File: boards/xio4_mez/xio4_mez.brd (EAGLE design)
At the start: 63 x 91 mm, 89 parts, among them IC1 SN74LVC2G07DCKR, IC2 SN74LVC1G07MDCKREP, IC3 NL17SZ126XV5T2G, IC4 TPS2051BDBVR, Q1 SMMBT3904LT1G

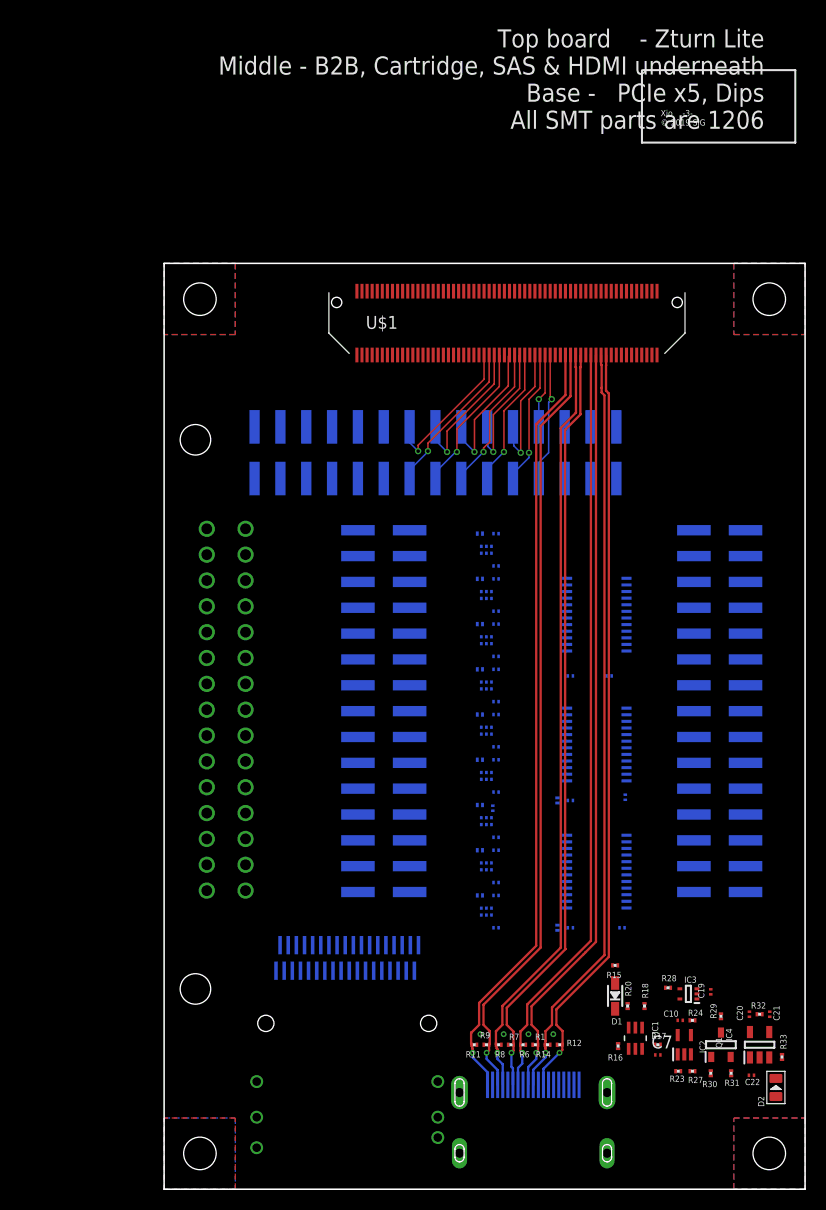
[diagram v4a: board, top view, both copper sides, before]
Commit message: Almost routed. Fixed tx100 net classes
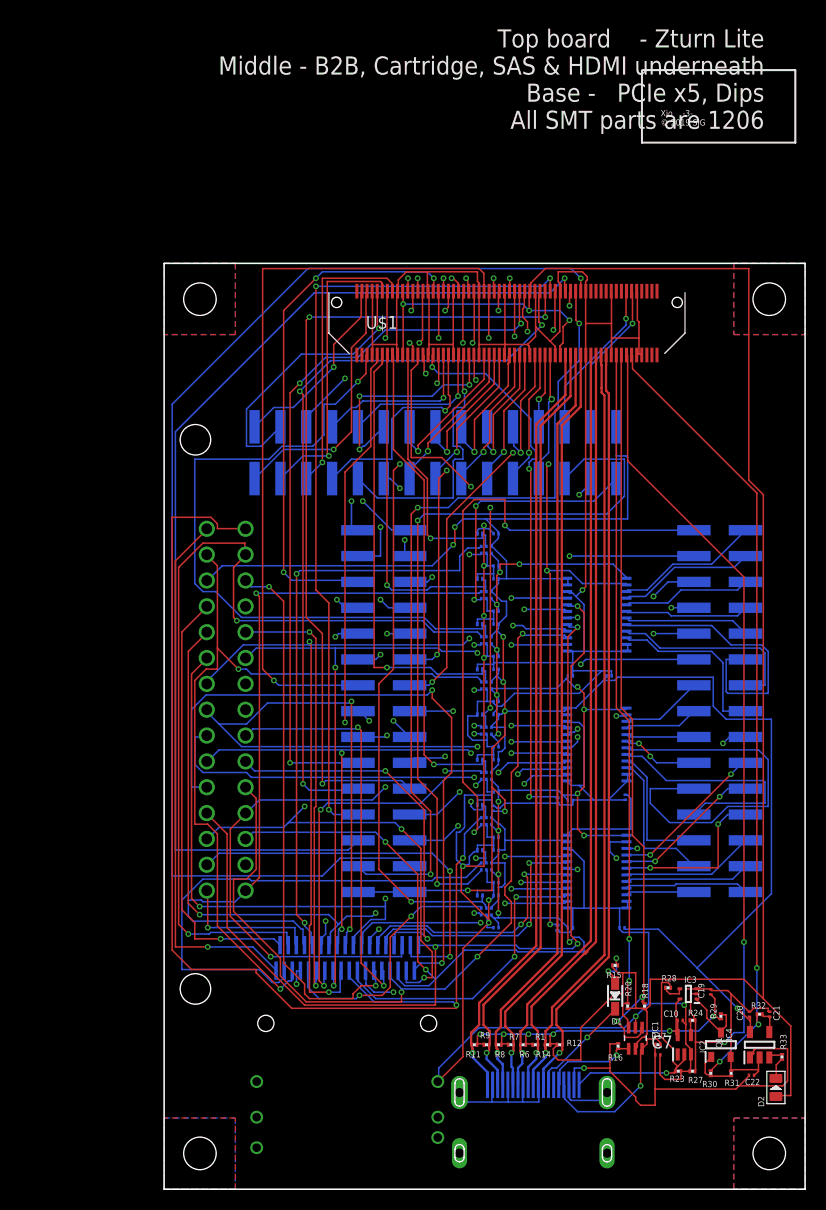
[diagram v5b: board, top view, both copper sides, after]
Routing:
- net GND: track 0.00 -> 444.9 mm, vias 0 -> 10
- net +5V: track 0.00 -> 240.1 mm, vias 0 -> 8
- net VCCIO: track 0.00 -> 219.8 mm, vias 4 -> 9
- net HBUS27: track 0.00 -> 118.1 mm, vias 0 -> 1
- net HI_CLK: track 0.00 -> 113.2 mm, vias 0 -> 2
- net +3V3: track 0.00 -> 107.7 mm, vias 0 -> 14
- net HBUS24: track 0.00 -> 105.3 mm, vias 0 -> 1
- net HI_A3: track 0.00 -> 97.5 mm, vias 0 -> 3
- net HI_A1: track 0.00 -> 92.9 mm, vias 0 -> 3
- net HI_R/!W!: track 0.00 -> 88.0 mm, vias 0 -> 2
- net HI_A6: track 0.00 -> 86.5 mm, vias 0 -> 3
- net HI_A4: track 0.00 -> 86.1 mm, vias 0 -> 4
- net HI_D1: track 0.00 -> 85.9 mm, vias 0 -> 4
- net HDMI_DET_IO: track 0.00 -> 85.0 mm, vias 0 -> 2
- net DIR_A: track 0.00 -> 84.4 mm, vias 0 -> 5
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- added copper zone on layer 2, net GND

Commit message: Fully routed board
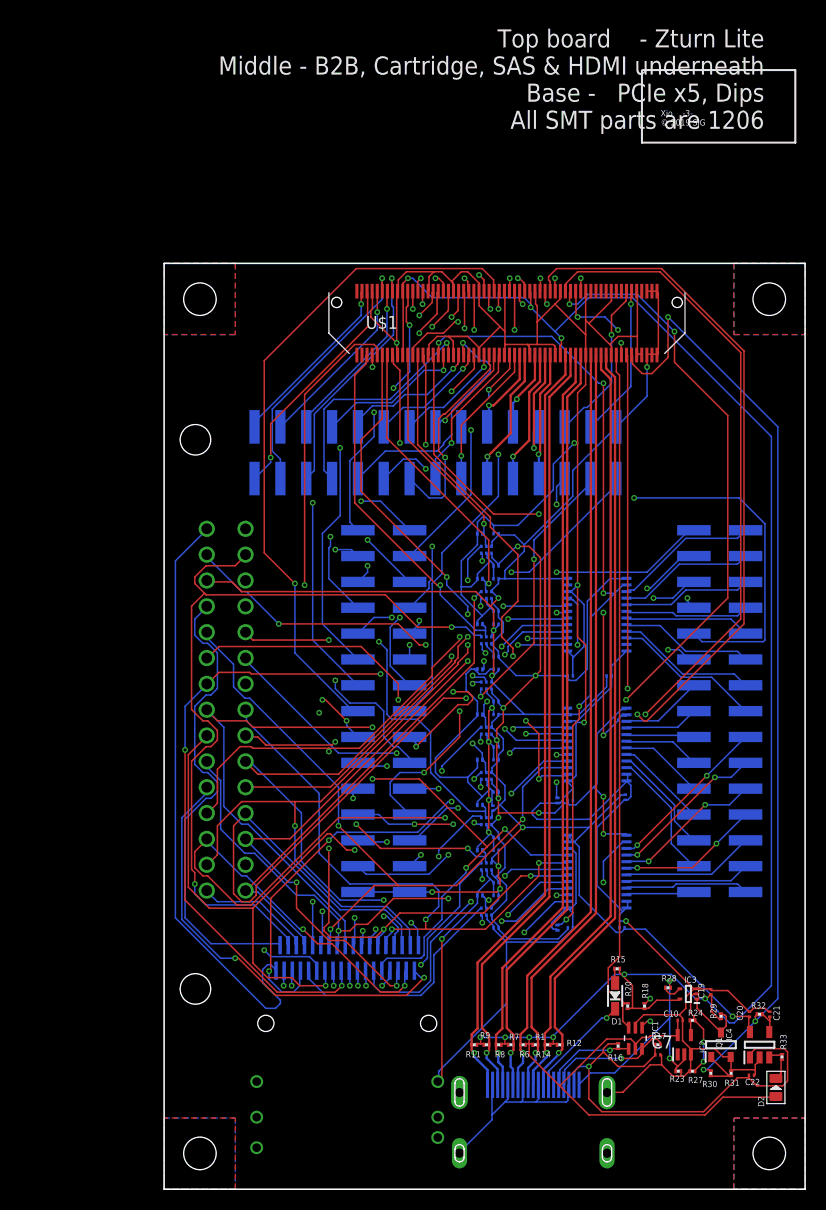
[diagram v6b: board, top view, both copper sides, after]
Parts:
- moved R15 0.39 mm to (44.5, 21.7), turned to 0 degrees
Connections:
- net +5V: now also U$1.115, U$1.116, U$1.117, U$1.118, U$1.119, U$1.120
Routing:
- net +5V: track 240.1 -> 194.9 mm, vias 8 -> 9
- net HBUS27: track 118.1 -> 74.6 mm, vias 1 -> 2
- net HI_CLK: track 113.2 -> 73.5 mm
- net DIR_RW: track 68.2 -> 35.0 mm
- net LO_D4: track 37.7 -> 8.28 mm
- net DIR_HALT: track 67.2 -> 96.5 mm, vias 3 -> 2
- net HI_A3: track 97.5 -> 69.1 mm
- net !LO_RST!: track 73.1 -> 45.1 mm
- net HI_RD4: track 73.3 -> 47.5 mm
- net !LO_IRQ!: track 26.5 -> 51.0 mm
- net HBUS21: track 81.4 -> 59.1 mm, vias 3 -> 2
- net HI_A4: track 86.1 -> 64.2 mm
- net DIR_CLK: track 76.6 -> 55.0 mm
- net !HI_RST!: track 49.3 -> 28.3 mm, vias 0 -> 2
- net HI_A9: track 77.4 -> 57.2 mm, vias 2 -> 3
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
